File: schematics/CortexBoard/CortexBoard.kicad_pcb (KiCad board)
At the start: 2 copper layers, 104.1 x 104.1 mm, 29 parts, among them J1 Cortex Serial CLI, J2 UART6 Connector, J3 Odroid Power, J4 Power Switch & LED, J5 LevelShifter_in, J6 LevelShifter-Out, J7 Cortex I2C CLI, P1 Power IN 3S 11.1, P2 BNO055, P3 D24V50F5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

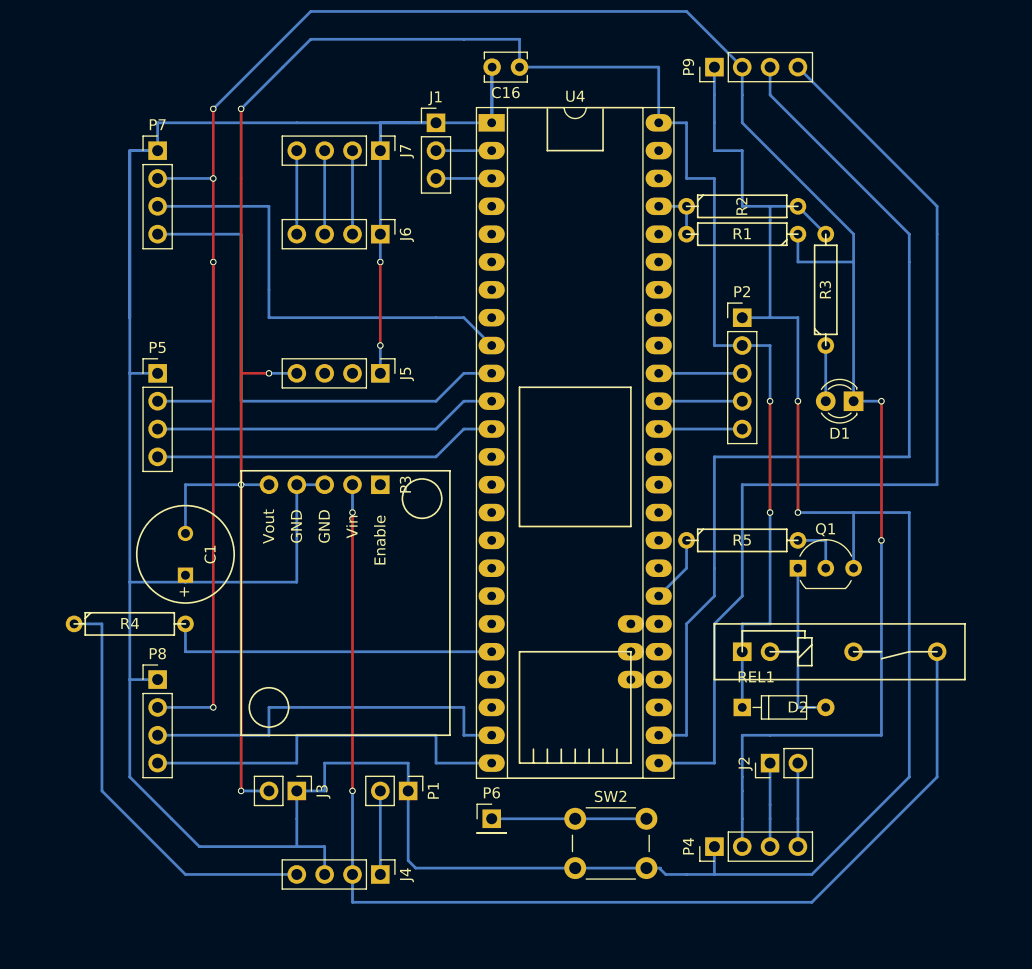
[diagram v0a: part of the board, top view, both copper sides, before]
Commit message: Body is too tight., gave it 5mm more headroom
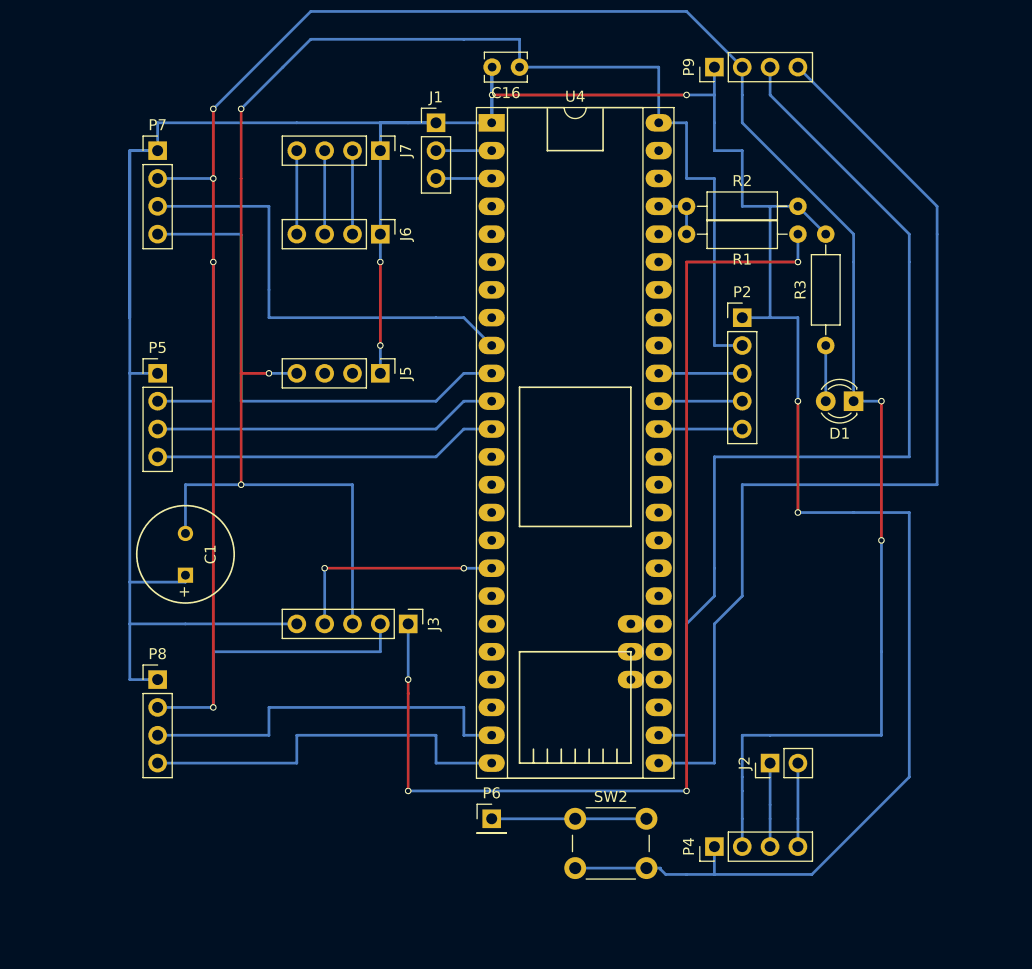
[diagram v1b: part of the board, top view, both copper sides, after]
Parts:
- removed D2: D_Schottky, Diodes_THT:D_DO-35_SOD27_P7.62mm_Horizontal
- removed J4: Power Switch & LED, Pin_Headers:Pin_Header_Straight_1x04_Pitch2.54mm
- removed P1: Power IN 3S 11.1, Pin_Headers:Pin_Header_Straight_1x02_Pitch2.54mm
- removed P3: D24V50F5, Cortex:Pololu_D24V50F5
- removed Q1: BC337(o.ä.), TO_SOT_Packages_THT:TO-92_Inline_Wide
- removed R4: 470, Discret:R4
- removed R5: 1K, Discret:R4
- removed REL1: HF49FD, Cortex:Relay_HF49FD
- J3: value Odroid Power -> CONN_01X05; footprint Pin_Headers:Pin_Header_Straight_1x02_Pitch2.54mm -> Pin_Headers:Pin_Header_Straight_1x05_Pitch2.54mm
- R1: value 82K -> 150K; footprint Discret:R4 -> Resistors_THT:R_Axial_DIN0207_L6.3mm_D2.5mm_P10.16mm_Horizontal
- R2: footprint Discret:R4 -> Resistors_THT:R_Axial_DIN0207_L6.3mm_D2.5mm_P10.16mm_Horizontal
- R3: value 4,7K -> 3.3K; footprint Discret:R4 -> Resistors_THT:R_Axial_DIN0207_L6.3mm_D2.5mm_P10.16mm_Horizontal
- moved J3 18.3 mm to (91.4, 114.3)
- moved R3 5.08 mm to (129.5, 88.9)
- moved R1 5.08 mm to (127.0, 78.7)
- moved R2 5.08 mm to (116.8, 76.2)
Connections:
- net /3.3V renamed /3.3V_ODroid
- C1 pad 1: GNDPWR -> /GND
- C16 pad 2: GNDPWR -> /GND
- D1 pad 1: /R7.4V -> /+10V
- J1 pad 1: GNDPWR -> /GND
- J3 pad 1: GNDPWR -> /+14V
- J3 pad 2: /+5V -> /+10V
- J5 pad 1: GNDPWR -> /GND
- J6 pad 1: GNDPWR -> /GND
- J7 pad 1: GNDPWR -> /GND
- P2 pad 1: GNDPWR -> /GND
- P4 pad 1: GNDPWR -> /GND
- P4 pad 2: /R7.4V -> /+10V
- P5 pad 1: GNDPWR -> /GND
- P5 pad 2: /R7.4V -> /+10V
- P7 pad 1: GNDPWR -> /GND
- P7 pad 2: /R7.4V -> /+10V
- P8 pad 1: GNDPWR -> /GND
- P8 pad 2: /R7.4V -> /+10V
- P9 pad 1: GNDPWR -> /GND
- P9 pad 2: /R7.4V -> /+10V
- R1 pad 1: /R7.4V -> /+14V
- R2 pad 2: GNDPWR -> /GND
- R3 pad 2: GNDPWR -> /GND
- SW2 pad 2: GNDPWR -> /GND
- U4 pad 1: GNDPWR -> /GND
- U4 pad 17: (no net) -> /Relay
- U4 pad 20: Net-(R4-Pad2) -> (no net)
- U4 pad 31: Net-(R5-Pad1) -> (no net)
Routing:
- net GNDPWR: track 381.6 -> 0.00 mm, vias 4 -> 0
- net /GND: track 0.00 -> 316.4 mm, vias 0 -> 6
- net /+10V: track 0.00 -> 250.0 mm, vias 0 -> 6
- net /R7.4V: track 237.3 -> 0.00 mm, vias 6 -> 0
- net /SWout_11.1V: track 107.6 -> 0.00 mm, vias 2 -> 0
- net /+14V: track 0.00 -> 101.6 mm, vias 0 -> 4
- net /+5V: track 196.3 -> 148.0 mm, vias 7 -> 4
- net /LEDAnode: track 38.7 -> 0.00 mm
- net Net-(R4-Pad2): track 30.5 -> 0.00 mm
- net /Relay: track 0.00 -> 20.3 mm, vias 0 -> 2
- net Net-(D2-Pad2): track 17.8 -> 0.00 mm
- net /SWin_11.1V: track 7.62 -> 0.00 mm
- net Net-(R5-Pad1): track 6.13 -> 0.00 mm
- net Net-(Q1-Pad2): track 5.08 -> 0.00 mm

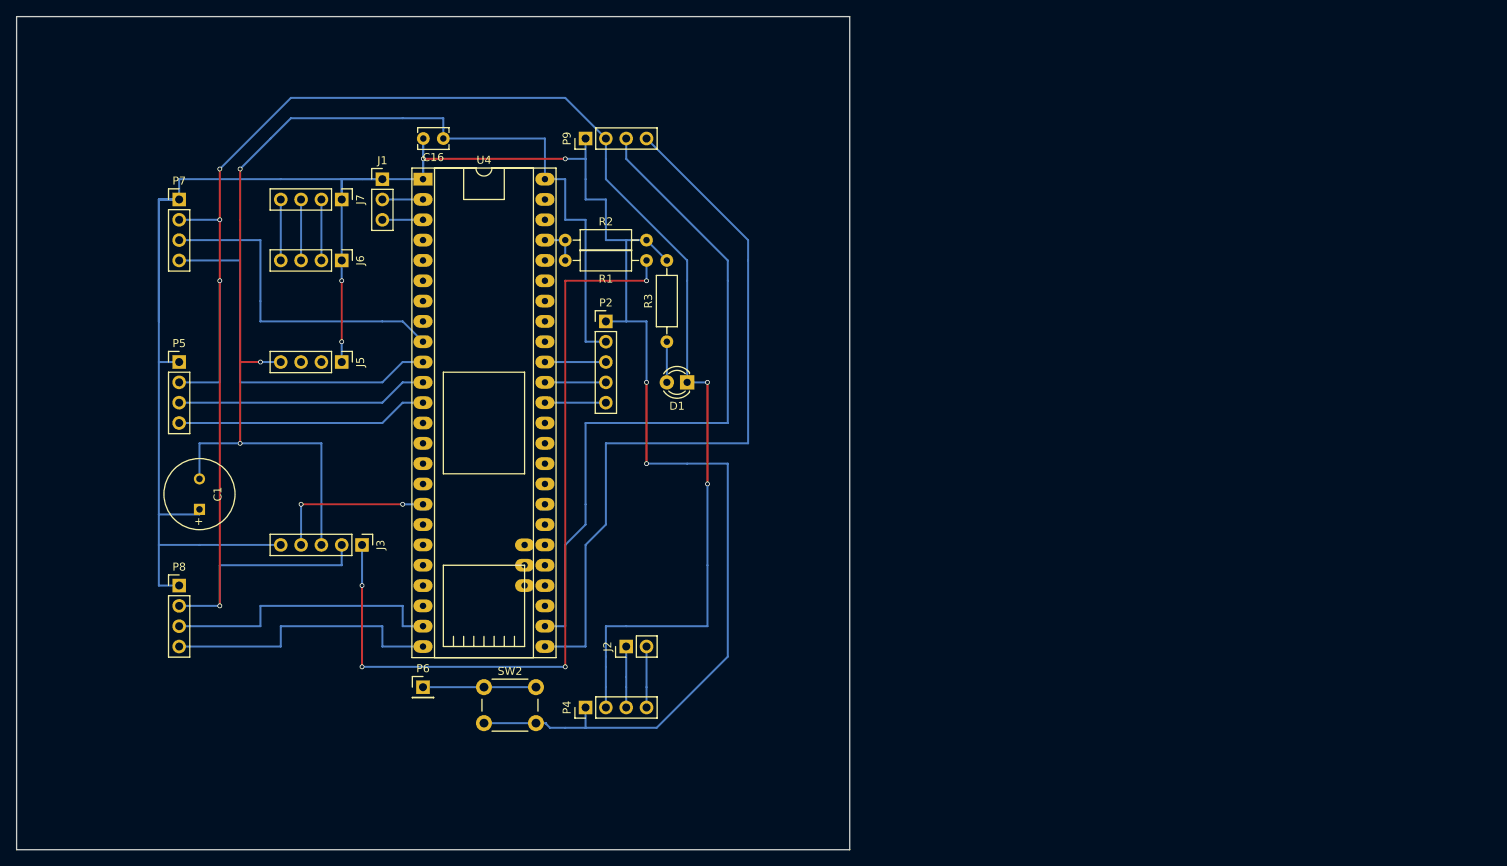
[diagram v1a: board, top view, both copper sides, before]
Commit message: corrected foot dampener, introduced design for Odroid XU4 and renamed old 040x stuff
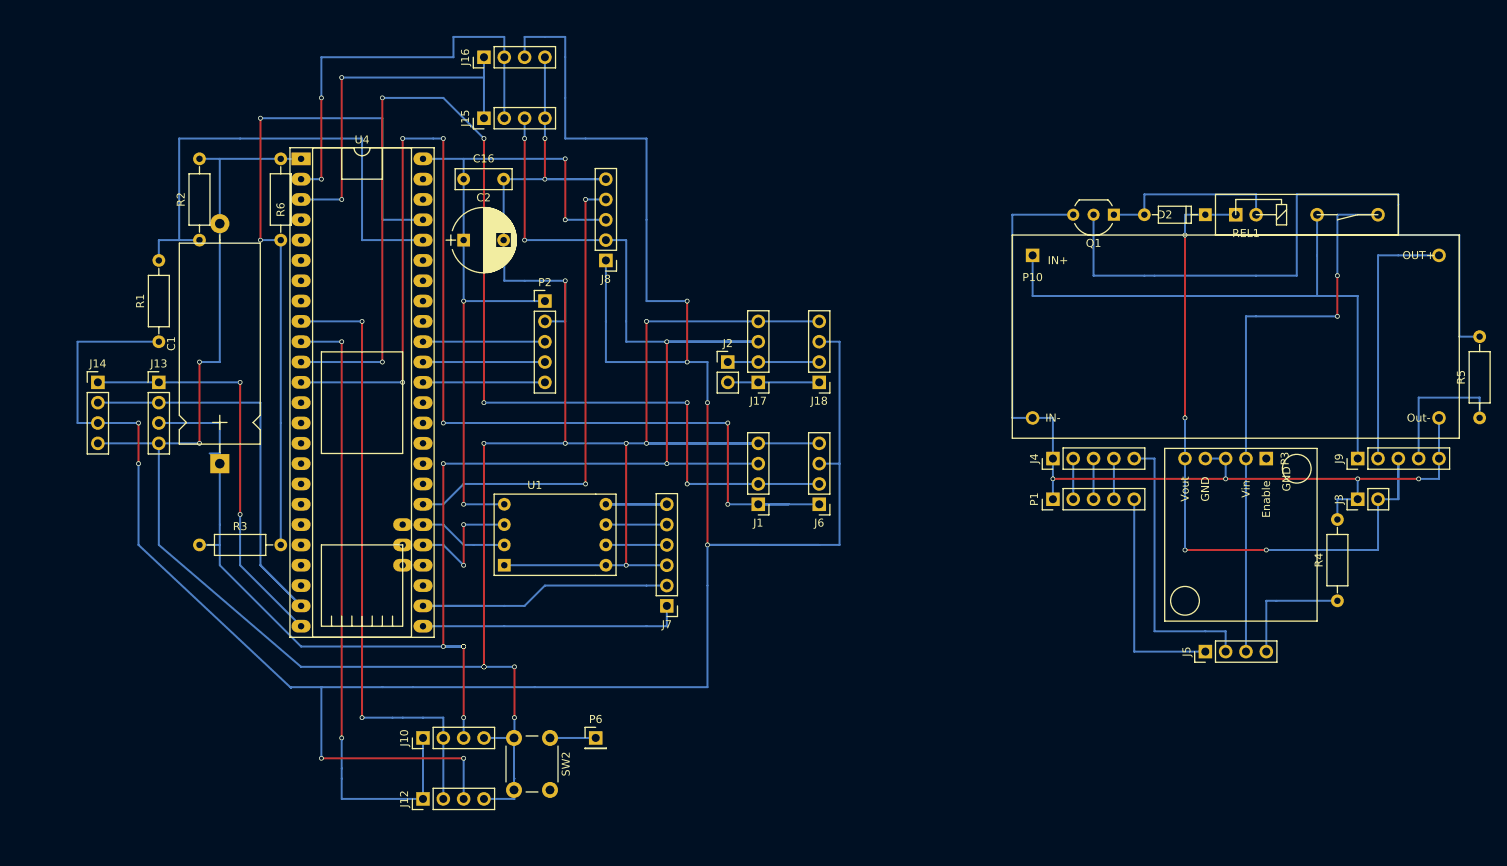
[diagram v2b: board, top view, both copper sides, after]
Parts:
- removed D1: LED, LEDs:LED_D3.0mm
- removed P4: LEG 5, Pin_Headers:Pin_Header_Straight_1x04_Pitch2.54mm
- removed P5: Leg 3, Pin_Headers:Pin_Header_Straight_1x04_Pitch2.54mm
- removed P7: Leg 2, Pin_Headers:Pin_Header_Straight_1x04_Pitch2.54mm
- removed P8: Leg 4, Pin_Headers:Pin_Header_Straight_1x04_Pitch2.54mm
- removed P9: Leg 1, Pin_Headers:Pin_Header_Straight_1x04_Pitch2.54mm
- added C2: 220uF, Capacitors_THT:CP_Radial_D8.0mm_P5.00mm, F.Cu at (104.1, 76.2)
- added D2: D_Schottky, Diodes_THT:D_DO-35_SOD27_P7.62mm_Horizontal, F.Cu at (196.8, 73.0)
- added J10: LEG2-LO, Pin_Headers:Pin_Header_Straight_1x04_Pitch2.54mm, F.Cu at (99.1, 138.4)
- added J12: LEG2-HI, Pin_Headers:Pin_Header_Straight_1x04_Pitch2.54mm, F.Cu at (99.1, 146.1)
- added J13: LEG3-LO, Pin_Headers:Pin_Header_Straight_1x04_Pitch2.54mm, F.Cu at (66.0, 94.0)
- added J14: LEG3-HI, Pin_Headers:Pin_Header_Straight_1x04_Pitch2.54mm, F.Cu at (58.4, 94.0)
- added J15: LEG4-LO, Pin_Headers:Pin_Header_Straight_1x04_Pitch2.54mm, F.Cu at (106.7, 61.0)
- added J16: LEG4-HI, Pin_Headers:Pin_Header_Straight_1x04_Pitch2.54mm, F.Cu at (106.7, 53.3)
- added J17: LEG5-LO, Pin_Headers:Pin_Header_Straight_1x04_Pitch2.54mm, F.Cu at (141.0, 94.0)
- added J18: LEG5-HI, Pin_Headers:Pin_Header_Straight_1x04_Pitch2.54mm, F.Cu at (148.6, 94.0)
- added J4: Bodysocket, Pin_Headers:Pin_Header_Straight_1x05_Pitch2.54mm, F.Cu at (177.8, 103.5)
- added J8: Cortex-Power-In, Pin_Headers:Pin_Header_Straight_1x05_Pitch2.54mm, F.Cu at (121.9, 78.7)
- added J9: Cortex-Power-Out, Pin_Headers:Pin_Header_Straight_1x05_Pitch2.54mm, F.Cu at (215.9, 103.5)
- added P1: Battery, Pin_Headers:Pin_Header_Straight_1x05_Pitch2.54mm, F.Cu at (177.8, 108.6)
- added P10: XL4015, Cortex:XL4015, F.Cu at (175.3, 83.2)
- added P3: D24V50F5, Cortex:Pololu_D24V50F5, F.Cu at (204.5, 103.5)
- added Q1: BC337(o.ä.), TO_SOT_Packages_THT:TO-92_Inline_Wide, F.Cu at (185.4, 73.0)
- added R4: 3.3K, Resistors_THT:R_Axial_DIN0207_L6.3mm_D2.5mm_P10.16mm_Horizontal, F.Cu at (213.4, 121.3)
- added R5: 1K, Resistors_THT:R_Axial_DIN0207_L6.3mm_D2.5mm_P10.16mm_Horizontal, F.Cu at (231.1, 98.4)
- added R6: 10K, Resistors_THT:R_Axial_DIN0207_L6.3mm_D2.5mm_P10.16mm_Horizontal, F.Cu at (81.3, 76.2)
- added REL1: HF49FD, Cortex:Relay_HF49FD, F.Cu at (200.7, 73.0)
- added U1: I2C_LevelShifter, Cortex:I2C_LevelShifter, F.Cu at (109.2, 109.2)
- C1: value 100uF -> 2200uF; footprint Discret:C1.5V8V -> Capacitors_THT:CP_Axial_L25.0mm_D10.0mm_P30.00mm_Horizontal
- C16: footprint Capacitors_THT:C_Disc_D3.8mm_W2.6mm_P2.50mm -> Capacitors_THT:C_Rect_L7.0mm_W2.5mm_P5.00mm
- J1: value Cortex Serial CLI -> LEG1-LO; footprint Pin_Headers:Pin_Header_Straight_1x03_Pitch2.54mm -> Pin_Headers:Pin_Header_Straight_1x04_Pitch2.54mm
- J3: value CONN_01X05 -> Odroid Power; footprint Pin_Headers:Pin_Header_Straight_1x05_Pitch2.54mm -> Pin_Headers:Pin_Header_Straight_1x02_Pitch2.54mm
- J5: value LevelShifter_in -> LED/Switch
- J6: value LevelShifter-Out -> LEG1-HI
- J7: value Cortex I2C CLI -> CORTEX CLI; footprint Pin_Headers:Pin_Header_Straight_1x04_Pitch2.54mm -> Pin_Headers:Pin_Header_Straight_1x06_Pitch2.54mm
- R3: value 3.3K -> 150K
- moved J3 124.6 mm to (215.9, 108.6), turned to 90 degrees
- moved J5 113.9 mm to (196.8, 127.6), turned to 90 degrees
- moved J6 67.0 mm to (148.6, 109.2), turned to 180 degrees
- moved J7 65.1 mm to (129.5, 121.9), turned to 180 degrees
- moved R3 63.7 mm to (71.1, 114.3), turned to 0 degrees
- moved J1 62.1 mm to (141.0, 109.2), turned to 180 degrees
- moved R1 61.8 mm to (66.0, 88.9), turned to 90 degrees
- moved R2 45.7 mm to (71.1, 76.2), turned to 90 degrees
- moved J2 37.8 mm to (137.2, 91.4), turned to 0 degrees
- moved P6 22.5 mm to (120.7, 138.4)
- moved U4 15.5 mm to (83.8, 66.0)
- moved SW2 10.4 mm to (114.9, 138.4), turned to 270 degrees
- moved P2 8.03 mm to (114.3, 83.8)
- moved C16 5.68 mm to (104.1, 68.6), turned to 0 degrees
- moved C1 4.58 mm to (73.7, 104.1)
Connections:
- C1 pad 1: /GND -> /+10V
- C1 pad 2: /+5V -> /GND
- C16 pad 1: /+5V -> /VIn+5V
- J1 pad 1: /GND -> /RX2
- J1 pad 2: /RX -> /TX2
- J1 pad 3: /TX -> /+10V
- J3 pad 1: /+14V -> /Batt-
- J3 pad 2: /+10V -> /+5V
- J5 pad 1: /GND -> /SW2/Batt
- J5 pad 2: /SDA0 -> /Batt+
- J5 pad 3: /SCL0 -> /SW1/VIN/LEDAnode
- J5 pad 4: /+5V -> /LEDKathode
- J6 pad 1: /GND -> /RX2
- J6 pad 2: /SDA-ODroid -> /TX2
- J6 pad 3: /SCL-ODroid -> /+14V
- J6 pad 4: /3.3V_ODroid -> /GND
- J7 pad 1: /GND -> /TX5
- J7 pad 2: /SDA-ODroid -> /RX5
- J7 pad 3: /SCL-ODroid -> /GND
- J7 pad 4: /3.3V_ODroid -> /SDA-ODroid
- P2 pad 1: /GND -> /VIn+5V
- P2 pad 2: /+5V -> /GND
- R3 pad 1: Net-(D1-Pad2) -> /+10V
- R3 pad 2: /GND -> Net-(R3-Pad2)
- U4 pad 17: /Relay -> (no net)
- U4 pad 2: /RX -> /TX1
- U4 pad 25: /RX5 -> /TX5
- U4 pad 26: /TX5 -> /RX5
- U4 pad 3: /TX -> /RX1
- U4 pad 31: (no net) -> /Relay-Out
- U4 pad 34: (no net) -> /GND
- U4 pad 44: (no net) -> Net-(R1-Pad2)
- U4 pad 45: Net-(R1-Pad2) -> Net-(R3-Pad2)
- U4 pad 48: /+5V -> /VIn+5V
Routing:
- net /+14V: track 101.6 -> 350.2 mm, vias 4 -> 8
- net /TX2: track 31.5 -> 152.0 mm, vias 0 -> 6
- net /RX2: track 31.5 -> 148.6 mm, vias 0 -> 6
- net /Batt-: track 0.00 -> 116.8 mm, vias 0 -> 4
- net /GND: track 316.4 -> 407.2 mm, vias 6 -> 16
- net /VIn+5V: track 0.00 -> 89.0 mm, vias 0 -> 5
- net Net-(R3-Pad2): track 0.00 -> 88.9 mm, vias 0 -> 2
- net Net-(Q1-Pad2): track 0.00 -> 83.8 mm
- net /Vout+14V: track 0.00 -> 76.2 mm
- net /SW1/VIN/LEDAnode: track 0.00 -> 71.1 mm, vias 0 -> 2
- net /Relay-Out: track 0.00 -> 59.5 mm, vias 0 -> 2
- net Net-(R1-Pad2): track 5.08 -> 64.1 mm
- net /+5V: track 148.0 -> 91.4 mm
- net /TX5: track 87.6 -> 33.0 mm
- net /RX5: track 92.7 -> 39.2 mm, vias 0 -> 1
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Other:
- board outline removed
